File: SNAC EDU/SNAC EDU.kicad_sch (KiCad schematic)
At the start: 0 parts

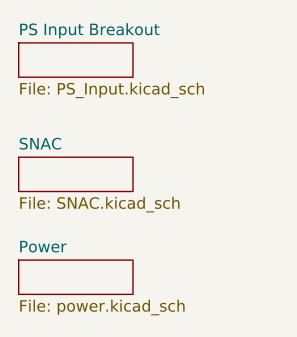
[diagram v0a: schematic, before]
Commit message: split the controller and levelshifter into 2 projects for easier manufacturing
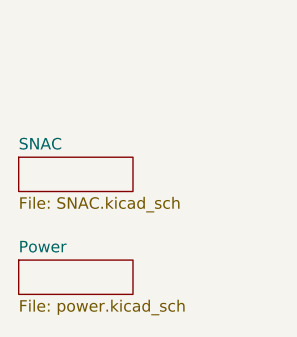
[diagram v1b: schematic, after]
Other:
- removed sheet PS Input Breakout
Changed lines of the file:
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@@
 	(generator "eeschema")
 	(generator_version "8.0")
-	(paper "B")
+	(paper "A")
 	(sheet
 		(at 52.07 59.69)
@@
 		)
 		(instances
-			(project "SuperStation one controller SNAC breakout"
+			(project "SNAC EDU"
 				(path "/cbd92933-d20e-42b7-906c-813e5f34c94a"
 					(page "4")
-				)
-			)
-		)
-	)
-	(sheet
-		(at 52.07 35.56)
-		(size 12.7 3.81)
-		(fields_autoplaced yes)
-		(stroke
-			(width 0.1524)
-			(type solid)
-		)
-		(fill
-			(color 0 0 0 0.0000)
-		)
-		(property "Sheetname" "PS Input Breakout"
-			(at 52.07 34.8484 0)
-			(effects
-				(font
-					(size 1.27 1.27)
-				)
-				(justify left bottom)
-			)
-		)
-		(property "Sheetfile" "PS_Input.kicad_sch"
-			(at 52.07 39.9546 0)
-			(effects
-				(font
-					(size 1.27 1.27)
-				)
-				(justify left top)
-			)
-		)
-		(instances
-			(project "SuperStation one controller SNAC breakout"
-				(path "/cbd92933-d20e-42b7-906c-813e5f34c94a"
-					(page "2")
 				)
 			)
@@
 		)
 		(instances
-			(project "SuperStation one controller SNAC breakout"
+			(project "SNAC EDU"
 				(path "/cbd92933-d20e-42b7-906c-813e5f34c94a"
 					(page "3")
